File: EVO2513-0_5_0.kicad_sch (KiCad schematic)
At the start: 43 parts, among them J1 1053101204, J2 1053101114, J3 10144517-043802LF, J4 1053102204, J5 1053091102, J6 1053091102, M1 78614150960, M2 78614150960, M3 78614150960, M4 78614150960, M5 78614150960, M6 78614150960

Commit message: Use KiCad standard footprints for chip resistors and capacitors
The imported Lattech R/C footprints have poor land patterns (the 0402s
use 0.635 mm circular pads) and cause tombstoning in assembly. Replace
all 139 chip resistors and capacitors with KiCad's standard IPC-7351
nominal footprints:

  Res 0402/0603/1206/2512 -> Resistor_SMD:R_xxxx_xxxxMetric (87)
  Cap 0402/0603/0805/1206/1210 -> Capacitor_SMD:C_xxxx_xxxxMetric (52)

Each part keeps its position, rotation, side, pad nets, schematic link
and reference/value text placement. The pads are on the same axis with
pad 1 on the same side, and every old pad centre lies inside the new
pad, so existing tracks still connect. Zones are refilled.

Schematic Footprint fields and the symbols' footprint filters point at
the new footprints, and the unused imported R/C footprints are removed
from the project library. Electrolytic capacitors are not changed.

DRC: 0 unconnected items, as before. Tracks, vias, zone outlines and
all other footprints are unchanged. 11 courtyard overlaps are new,
because the old footprints had no courtyards.

Co-Authored-By: Claude Opus 5.5 <noreply@anthropic.com>
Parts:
- R28: footprint EVO2513-0_5_0-import-fps:Res 0402 H0-45 R -> Resistor_SMD:R_0402_1005Metric
- TH1, TH2: footprint EVO2513-0_5_0-import-fps:Res 0603 H0-45 -> Resistor_SMD:R_0603_1608Metric
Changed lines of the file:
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@@
 			)
 		)
-		(property "Footprint" "EVO2513-0_5_0-import-fps:Res 0402 H0-45 R"
+		(property "Footprint" "Resistor_SMD:R_0402_1005Metric"
 			(at 231.14 172.5422 0)
 			(hide yes)
@@
 			)
 		)
-		(property "Footprint" "EVO2513-0_5_0-import-fps:Res 0603 H0-45"
+		(property "Footprint" "Resistor_SMD:R_0603_1608Metric"
 			(at 269.24 172.5422 0)
 			(hide yes)
@@
 			)
 		)
-		(property "Footprint" "EVO2513-0_5_0-import-fps:Res 0603 H0-45"
+		(property "Footprint" "Resistor_SMD:R_0603_1608Metric"
 			(at 259.08 172.5422 0)
 			(hide yes)

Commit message: Fix schematic ERC issues from the import
ERC across all seven sheets reported 1481 issues from the import:

- Every item sat 43 mil off KiCad's 50 mil connection grid in Y, so new
  wires would not snap to existing pins. Each sheet's contents are
  shifted 7 mil (0.1778 mm) onto the grid; the library symbol
  definitions are untouched and a uniform shift keeps every connection.
  A few wire corners on S06 were off grid on their own (at 6740 mil,
  7620 mil and y 3290 mil); they move to the nearest grid point, which
  removes two 10 mil stubs and moves #PWR065 with its wire.
- Nine wires ran 1.27-2.54 mm past the label sitting on them (ID on S01;
  LDVR1/2 and HDVR1/2 on S06), leaving dangling ends. They are trimmed
  back to the label.
- GND, +12V, +3V3MCU and +5V enter through connector pins, so ERC had
  no power source for them. A PWR_FLAG (#FLG01-#FLG04) sits on each.
- The title-block module name used the Altium formula
  ${COPY(DOCUMENTNAME,5,LENGTH(DOCUMENTNAME)-11)}, which KiCad cannot
  evaluate. Each sheet now carries the title it produced.

ERC: 1481 -> 0. The netlist still matches the PCB's 147 nets.

Update PCB from Schematic was rerun afterwards. It changes metadata only:
footprint filters, unit and pin-function data from the symbols, and the
KiLib_Generator fields dropped from the 139 standard R/C footprints. No
placement or copper changes.

Co-Authored-By: Claude Opus 5.5 <noreply@anthropic.com>
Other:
- note added: "External Connectors"
- note removed: "${COPY(DOCUMENTNAME,5,LENGTH(DOCUMENTNAME)-11)}"

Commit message: Convert the schematic to a hierarchical root sheet
The Altium import produced seven KiCad 10 top-level sheets, with S01's
content in EVO2513-0_5_0.kicad_sch. kicad-cli only loads the first of
those, so command-line ERC, netlist and DRC parity checks saw S01 alone.

- EVO2513-0_5_0.kicad_sch is now a root sheet holding one sheet symbol per
  sheet; S01's content moves to "S01 External Connectors.kicad_sch".
- Each sheet symbol keeps its old top-level sheet UUID, so symbol
  references, net names and connectivity are unchanged: the netlist from
  the new root is identical to the previous whole-design netlist (229
  components, 147 nets). Cross-sheet nets still use global labels.
- The board's 229 footprint paths take the hierarchical form
  /<sheet>/<symbol>, and S01's footprints point at the new sheet file.
  No copper or placement changes.
- Every title block read "sheet 7 of 7" (a single DOCUMENTNUMBER project
  variable). Sheet numbers now use the page number: the root is page 1
  and S01-S07 are pages 2-8.

kicad-cli ERC over the whole design: 0 errors, 0 warnings. DRC with
schematic parity: 0 parity issues, 450 violations as before.

Co-Authored-By: Claude Opus 5.5 <noreply@anthropic.com>
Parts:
- removed BON1, BON10, BON11, BON12, BON13, BON14, BON15, BON16, BON17, BON18, BON19, BON2, BON20, BON21, BON22, BON23, BON24, BON25, BON26, BON3, BON4, BON5, BON6, BON7, BON8, BON9: POGO-1, EVO2513-0_5_0-import-fps:TEST PIN BON 1-25mm SMD Pad (POGO-1), symbol Lattech Systems:Test Pin BON 1-25mm SMD Pad (POGO-1)
- removed Fiducial1, Fiducial2: Fiducial, EVO2513-0_5_0-import-fps:Fiducial-50, symbol Lattech Systems:Fiducial
- removed J1: 1053101204, EVO2513-0_5_0-import-fps:Connector Molex 105310xx04 4POS 2.5mm THP, symbol Lattech Systems:Connector Molex 1053101204 2x2-Way 2.5mm Pitch THP
- removed J2: 1053101114, EVO2513-0_5_0-import-fps:CONNECTOR MOLEX 1053101114 2.5MM THP, symbol Lattech Systems:Connector Molex 1053101114 14-Way 2.5mm Pitch THP Vert
- removed J3: 10144517-043802LF, EVO2513-0_5_0-import-fps:Connector Amphenol BergStak 10144517-043802LF 40-Pin Receptical, symbol Lattech Systems:Connector Amphenol BergStak 10144517-043802LF 40-Pin Receptical
- removed J4: 1053102204, EVO2513-0_5_0-import-fps:Connector Molex 105310xx04 4POS 2.5mm THP, symbol Lattech Systems:Connector Molex 1053102204 2x2-Way 2.5mm Pitch THP
- removed J5, J6: 1053091102, EVO2513-0_5_0-import-fps:CONNECTOR MOLEX 1053091102 2POS 2.5MM THP, symbol Lattech Systems:Connector Molex 1053091102 2-Way 2.5mm Pitch THP
- removed M1: 78614150960, EVO2513-0_5_0-import-fps:Mech Spacer Wurth 78614150960 Through M3, symbol Lattech Systems:Mech Spacer Wurth 78614150960 Through M3 15mm
- removed M2, M3, M4, M5, M6: 78614150960, EVO2513-0_5_0-import-fps:MECH SPACER WURTH 78614150960 THROUGH M3, symbol Lattech Systems:Mech Spacer Wurth 78614150960 Through M3 15mm
- removed R28: 10K, Resistor_SMD:R_0402_1005Metric, symbol Lattech Systems:Resistor 10K 1% 0402
- removed TH1, TH2: 10k, Resistor_SMD:R_0603_1608Metric, symbol Lattech Systems:NTC Thermistor 10k 0603
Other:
- added sheet S01 External Connectors (S01 External Connectors.kicad_sch)
- added sheet S02 Input Protection (S02 Input Protection.kicad_sch)
- added sheet S03 BMS Input and Output Monitor (S03 BMS Input and Output Monitor.kicad_sch)
- added sheet S04 Charger Regulation (S04 Charger Regulation.kicad_sch)
- added sheet S05 Battery Management (S05 Battery Management.kicad_sch)
- added sheet S06 STEP-Up Step-Down Reg (S06 STEP-Up Step-Down Reg.kicad_sch)
- added sheet S07 Load Switch and I-Sense (S07 Load Switch and I-Sense.kicad_sch)
- note removed: "${##}"
- note removed: "${BOARD_NUMBER}"
- note removed: "${CURRENT_DATE}"
- note removed: "${DOCUMENTNUMBER}"
- note removed: "${PRODUCT_NAME}"
- note removed: "${SCH_REVISION}"
- note removed: "1"
- note removed: "2"
- note removed: "3"
- note removed: "4"
- note removed: "5"
- note removed: "6"
- note removed: "7"
- note removed: "8"
- note removed: "9"
- note removed: "A"
- note removed: "B"
- note removed: "C"
- note removed: "D"
- note removed: "DATE:"
- note removed: "Denotes Layout instructions"
- note removed: "Denotes text on the Identification layer on the PCB"
- note removed: "E"
- note removed: "External Connectors"
- note removed: "F"
- note removed: "G"
- note removed: "MODULE:"
- note removed: "OF"
- note removed: "PCB NUMBER:"
- note removed: "PRODUCT NAME:"
- note removed: "REVISION:"
- note removed: "SHEET NUMBER"
- company: (none) -> ${COMP_NAME}
- title: (none) -> EvoOne BMS (EVO2513 v0.5.0)

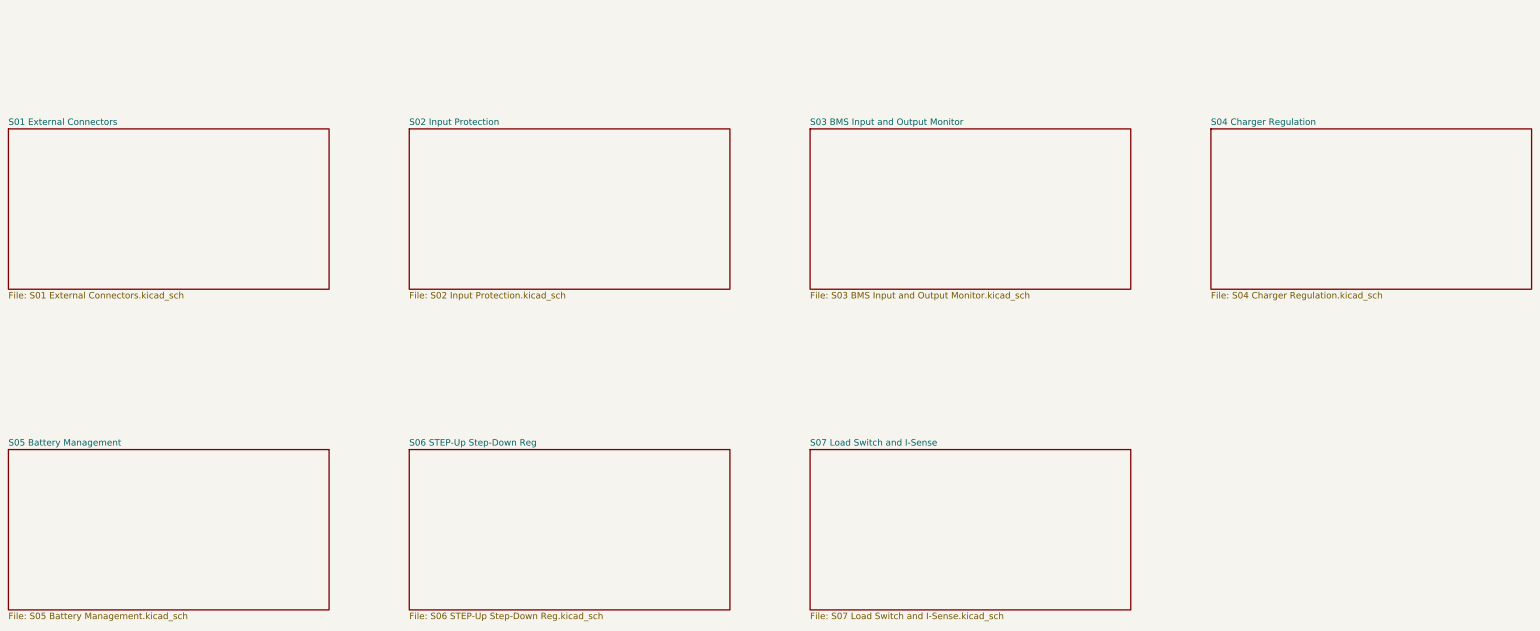
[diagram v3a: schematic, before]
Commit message: Link the sheets through hierarchical labels and sheet pins
The 78 cross-sheet global labels on S01-S07 become hierarchical labels,
and each sheet symbol on the root gets a pin per label name (71 pins).
On the root, each pin connects through a short wire to a global label
with the net name. Global labels there, rather than local ones, keep the
35 net names free of a "/" sheet-path prefix, so the net classes and the
board's nets are unchanged.

Layout: S01 External Connectors on the left with its pins on the right
edge; S02-S04 and S05-S07 in two columns with their pins on the left.

The netlist is identical to before (229 components, 147 nets, same names
and pins). kicad-cli ERC: 0 errors, 0 warnings. DRC with schematic
parity: 0 parity issues, 450 violations as before.

Co-Authored-By: Claude Opus 5.5 <noreply@anthropic.com>
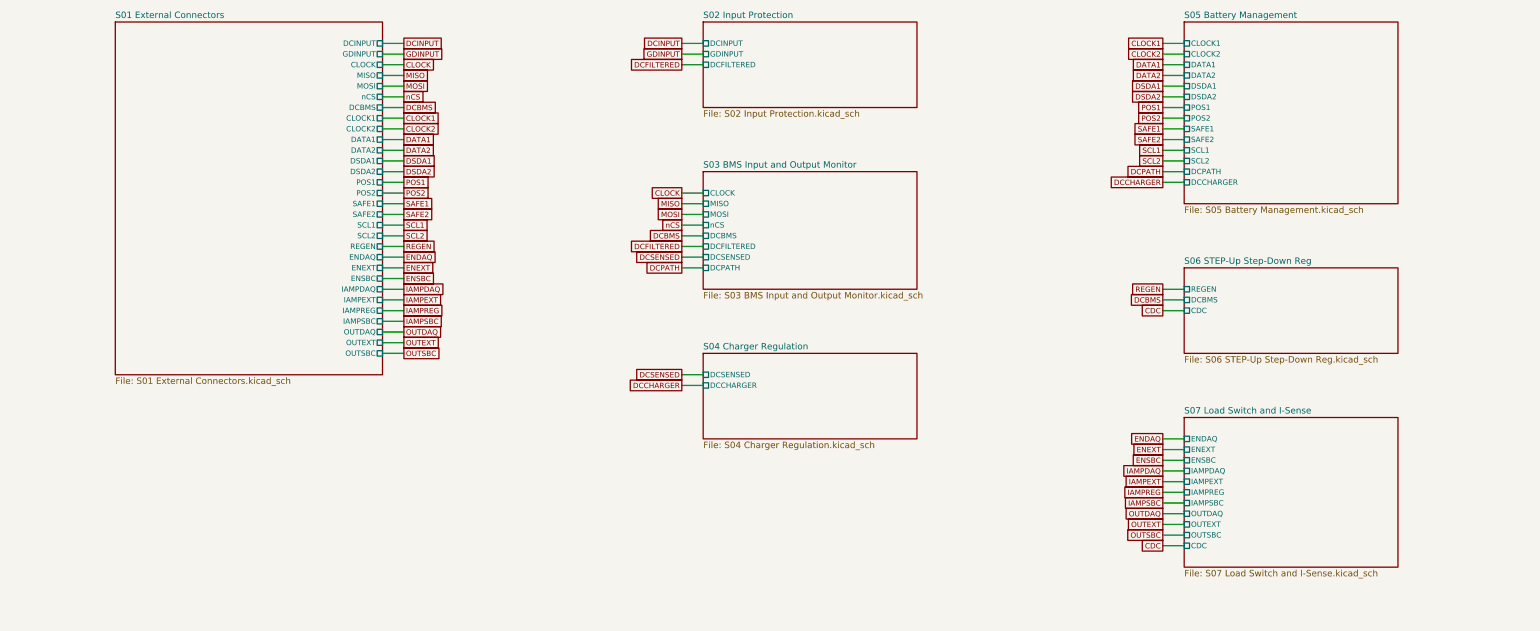
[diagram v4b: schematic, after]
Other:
- sheet S01 External Connectors ports: added CLOCK, CLOCK1, CLOCK2, DATA1, DATA2, DCBMS, DCINPUT, DSDA1, DSDA2, ENDAQ, ENEXT, ENSBC, GDINPUT, IAMPDAQ, IAMPEXT, IAMPREG, IAMPSBC, MISO, MOSI, OUTDAQ, OUTEXT, OUTSBC, POS1, POS2, REGEN, SAFE1, SAFE2, SCL1, SCL2, nCS; removed none
- sheet S02 Input Protection ports: added DCFILTERED, DCINPUT, GDINPUT; removed none
- sheet S03 BMS Input and Output Monitor ports: added CLOCK, DCBMS, DCFILTERED, DCPATH, DCSENSED, MISO, MOSI, nCS; removed none
- sheet S04 Charger Regulation ports: added DCCHARGER, DCSENSED; removed none
- sheet S05 Battery Management ports: added CLOCK1, CLOCK2, DATA1, DATA2, DCCHARGER, DCPATH, DSDA1, DSDA2, POS1, POS2, SAFE1, SAFE2, SCL1, SCL2; removed none
- sheet S06 STEP-Up Step-Down Reg ports: added CDC, DCBMS, REGEN; removed none
- sheet S07 Load Switch and I-Sense ports: added CDC, ENDAQ, ENEXT, ENSBC, IAMPDAQ, IAMPEXT, IAMPREG, IAMPSBC, OUTDAQ, OUTEXT, OUTSBC; removed none

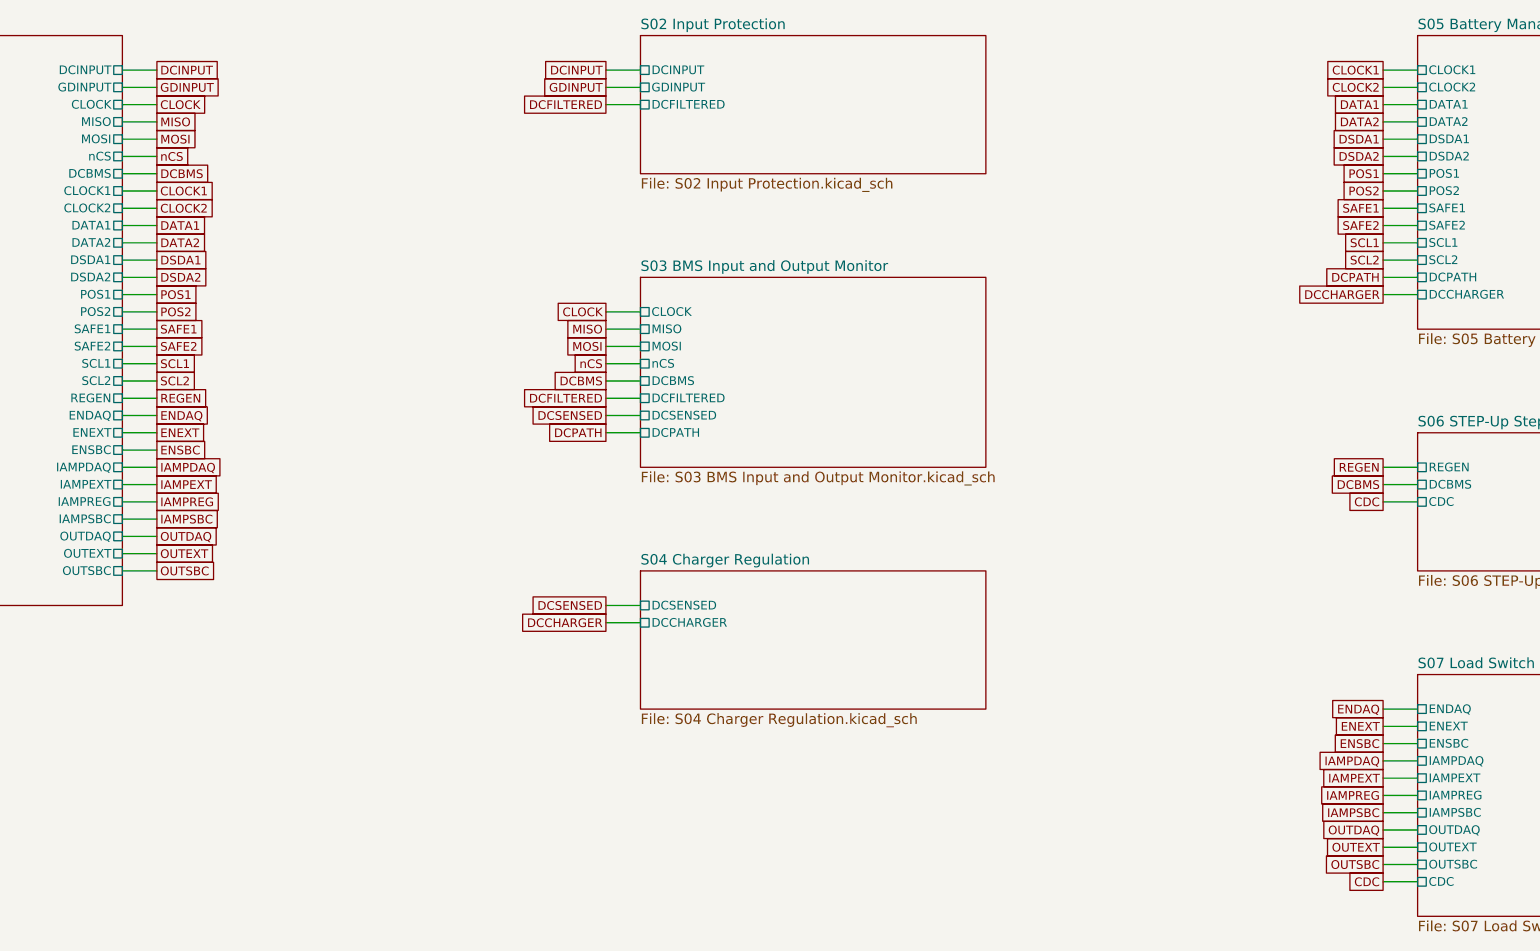
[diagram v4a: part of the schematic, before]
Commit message: Replace the root sheet's global labels with local labels
The root sheet joined the sheet pins with 71 global labels. They are now
local labels on short wire stubs, so the design has no global labels.

Nets are named by their highest-level label, so the 35 cross-sheet nets
now carry the root path: DCBMS becomes /DCBMS, POS1 becomes /POS1, and so
on. The 16 net class patterns that named them, and the board's 1402 net
references, are renamed to match. Connectivity is unchanged (147 nets,
same pins), and every net keeps its net class.

kicad-cli ERC: 0 errors, 0 warnings. DRC with schematic parity: 0 parity
issues, 450 violations as before.

Co-Authored-By: Claude Opus 5.5 <noreply@anthropic.com>
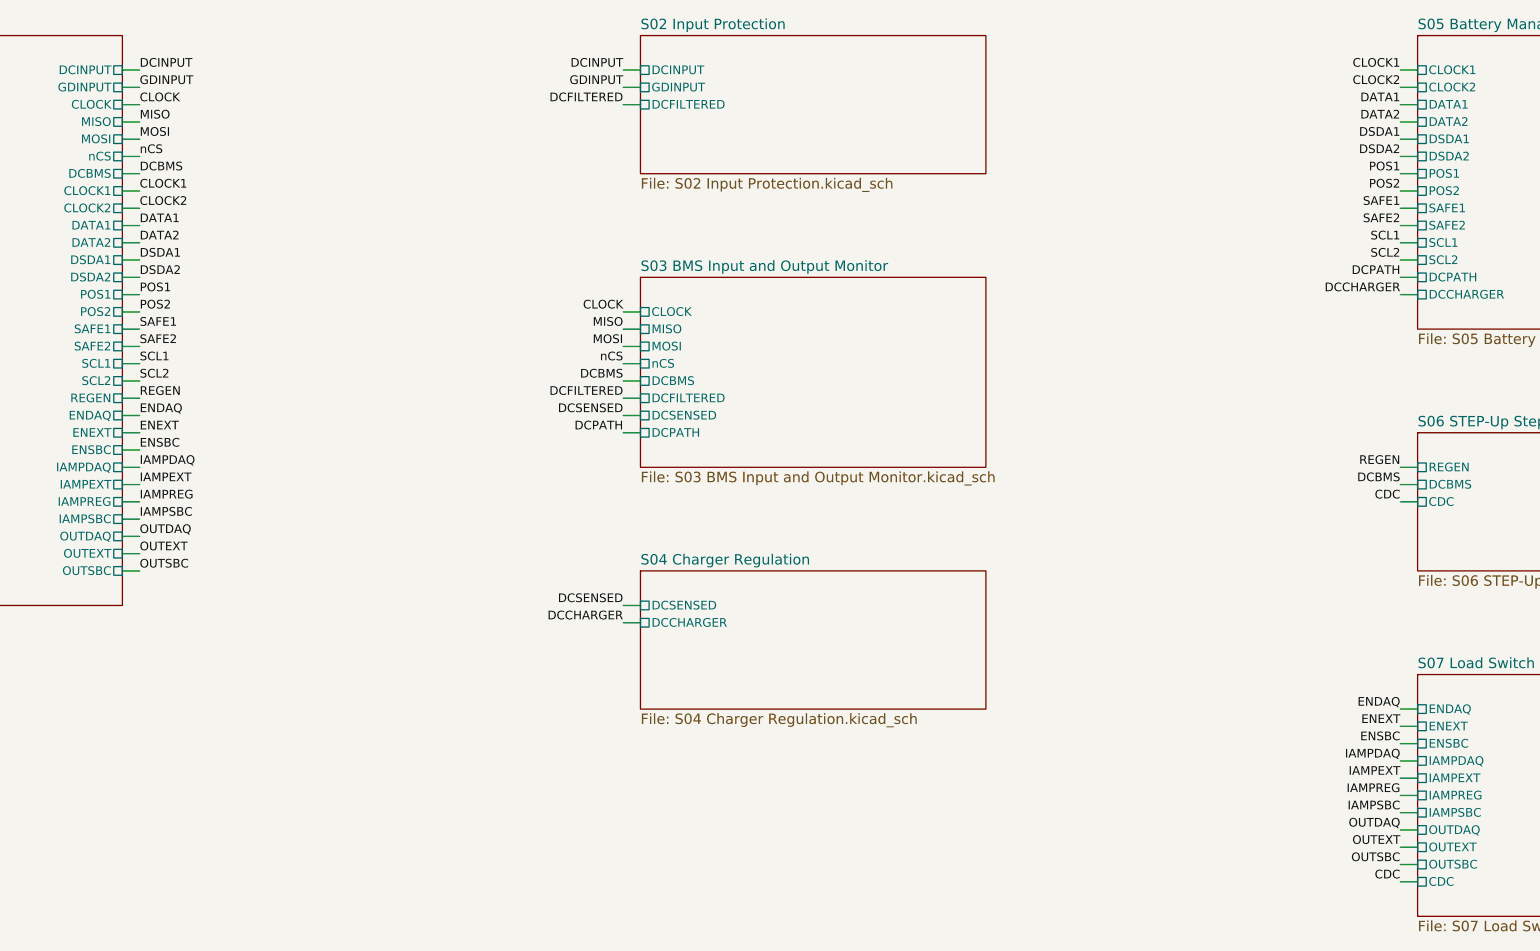
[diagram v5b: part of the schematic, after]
